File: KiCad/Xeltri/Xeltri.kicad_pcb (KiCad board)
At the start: 6 copper layers, 100 x 100 mm, 188 parts, among them J1 PJ-035DH, J2 877159106, J3 HR911105A_C12074, Q1 AOD407, U1 XC7A35T-CSG325, U10 SY8843QWC, U11 RT9013-18GB, U12 RT9013-12GB, U13 TPS22966DPUR, U14 TPS22966DPUR, U15 TPS22966DPUR, U16 TPS22966DPUR, U17 CH334P, U2 V851S, U3 TPS56637RPAR, U4 TPS56637RPAR, U5 STM32H745XIHx, U6 RTL8201F-VB-CG, U7 SY8843QWC, U8 SY8843QWC, U9 SY8843QWC, Y1 25Mhz

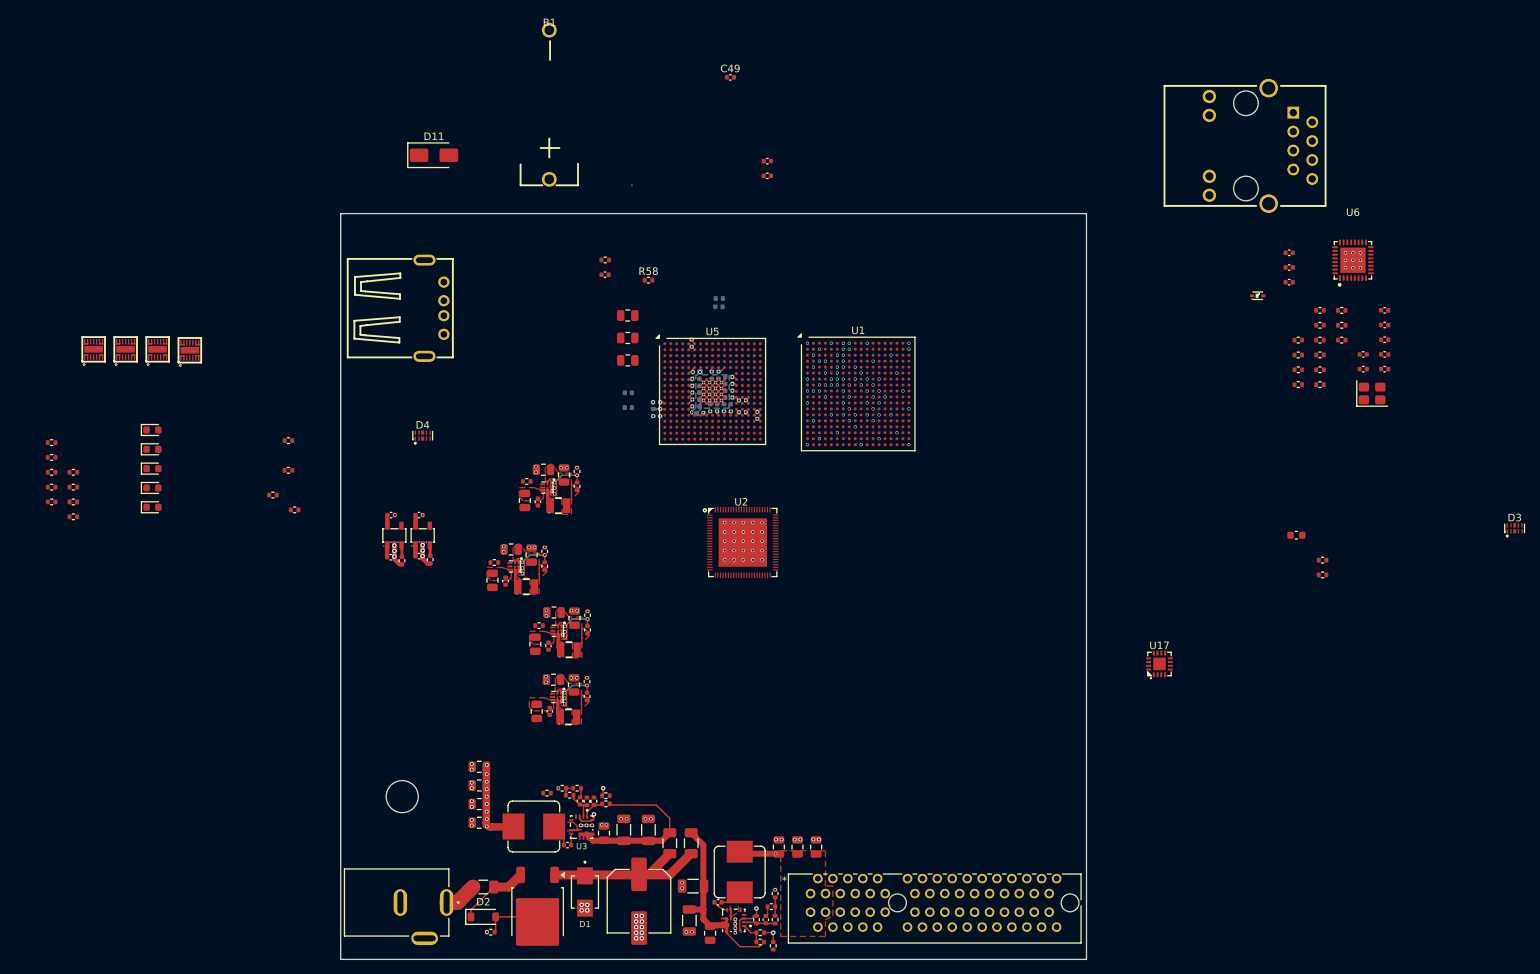
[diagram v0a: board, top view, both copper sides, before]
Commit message: Lay out STM32 power decoupling and add USB FS plus 24 V CIN ceramics.
USB VDD33/VDD50 share local 100 nF + 1 µF on 3.3 V; VBAT keeps a local 100 nF until the cell and diode are placed.

Co-authored-by: Cursor <cursoragent@cursor.com>
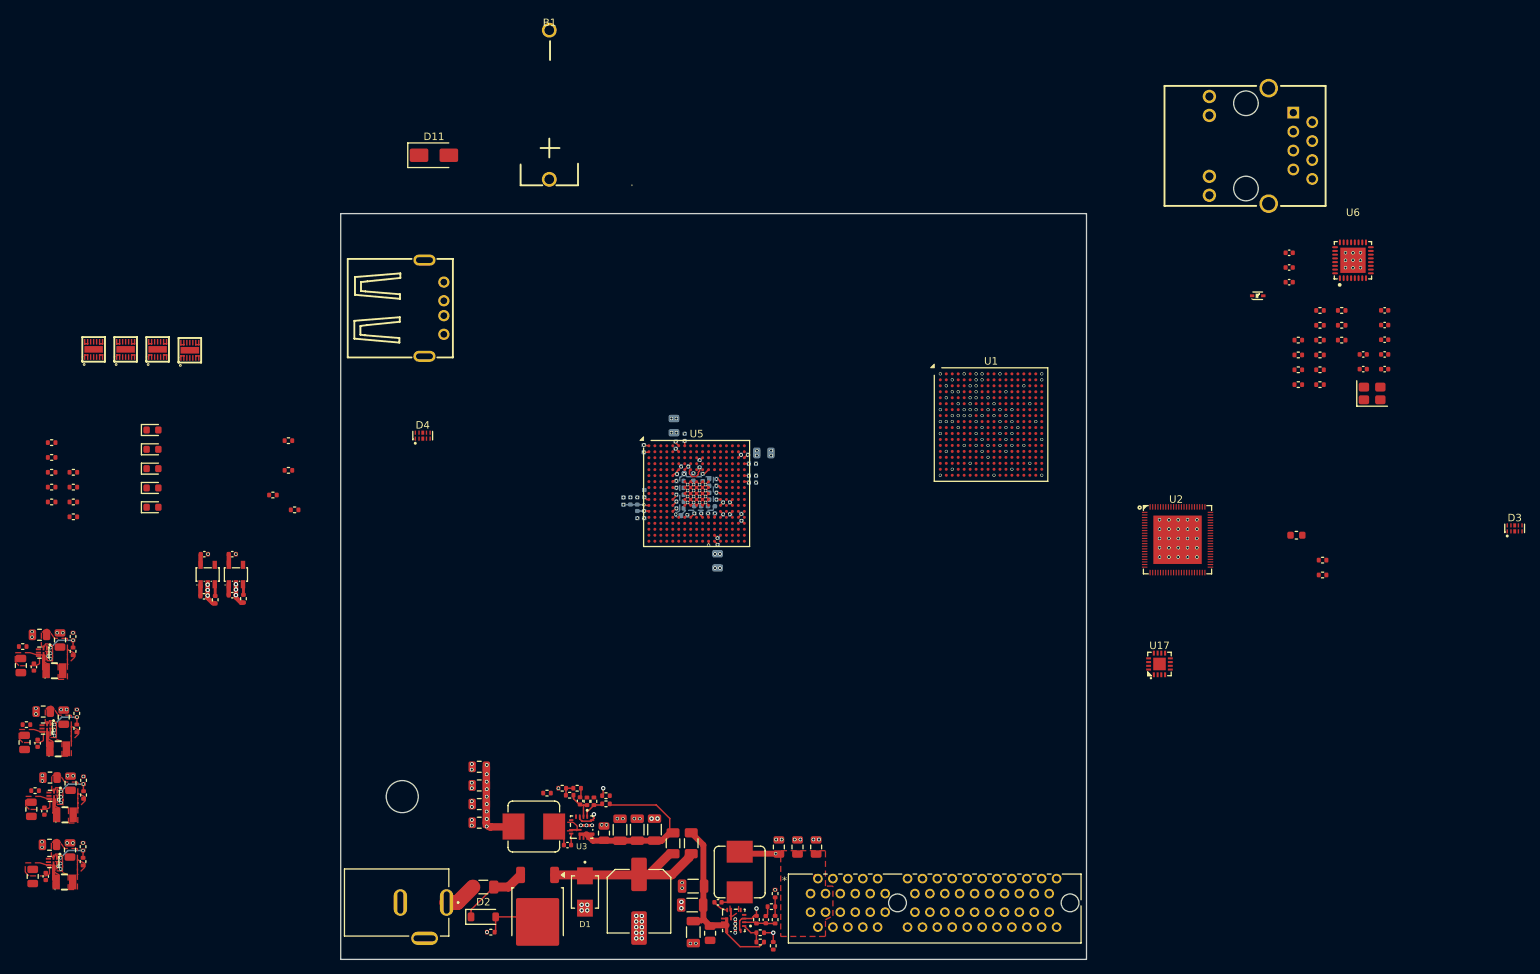
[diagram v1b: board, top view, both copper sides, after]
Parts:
- added C83: 10uF/50V, Capacitor_SMD:C_1206_3216Metric, F.Cu at (140.9, 138.5)
- added C84: 10uF/50V, Capacitor_SMD:C_1206_3216Metric, F.Cu at (135.8, 128.4)
- added C85: 100nF/16V, Capacitor_SMD:C_0402_1005Metric, B.Cu at (149.0, 81.0)
- added C86: 1uF/25V, Capacitor_SMD:C_0402_1005Metric, B.Cu at (149.0, 81.9)
- C49, C53, C54, C76, C77, C78, C82, R58, R61: moved to B.Cu
- moved C32 71.1 mm to (52.3, 125.7)
- moved C33 71.1 mm to (54.0, 125.9)
- moved C34 71.1 mm to (57.5, 122.2)
- moved C46 71.1 mm to (54.8, 121.4)
- moved L4 71.1 mm to (56.8, 126.4)
- moved R34 71.1 mm to (59.3, 121.8)
- moved R53 71.1 mm to (52.8, 123.2)
- moved U8 71.1 mm to (55.3, 123.8)
- moved C29 71.1 mm to (57.5, 131.2)
- moved C30 71.1 mm to (54.2, 134.7)
- moved C31 71.1 mm to (52.5, 134.7)
- moved C38 71.1 mm to (50.9, 106.4)
- moved C39 71.1 mm to (52.6, 106.6)
- moved C40 71.1 mm to (56.1, 103.0)
- moved C45 71.1 mm to (54.7, 130.5)
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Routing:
- net Net-(U5-BOOT0): track 0.00 -> 3.13 mm, vias 0 -> 1
- net VDDA: track 0.68 -> 3.45 mm, vias 1 -> 2
- net +3.3V: track 14.0 -> 16.5 mm, vias 22 -> 33
- net GND: track 45.2 -> 47.5 mm, vias 219 -> 239
- net Net-(C50-Pad2): track 0.00 -> 1.79 mm, vias 0 -> 3
- net Net-(U5-NRST): track 0.00 -> 0.72 mm, vias 0 -> 1
- net Net-(D11-K): track 0.00 -> 0.71 mm, vias 0 -> 1
- net Net-(U5-PDR_ON): track 0.00 -> 0.64 mm, vias 0 -> 1
- added copper zone on In3.Cu, net +3.3V
- added copper zone on In3.Cu, net Net-(C50-Pad2)

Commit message: Match the six-layer stackup to JLC06161H-3313 and update FPGA power wiring.
Co-authored-by: Cursor <cursoragent@cursor.com>
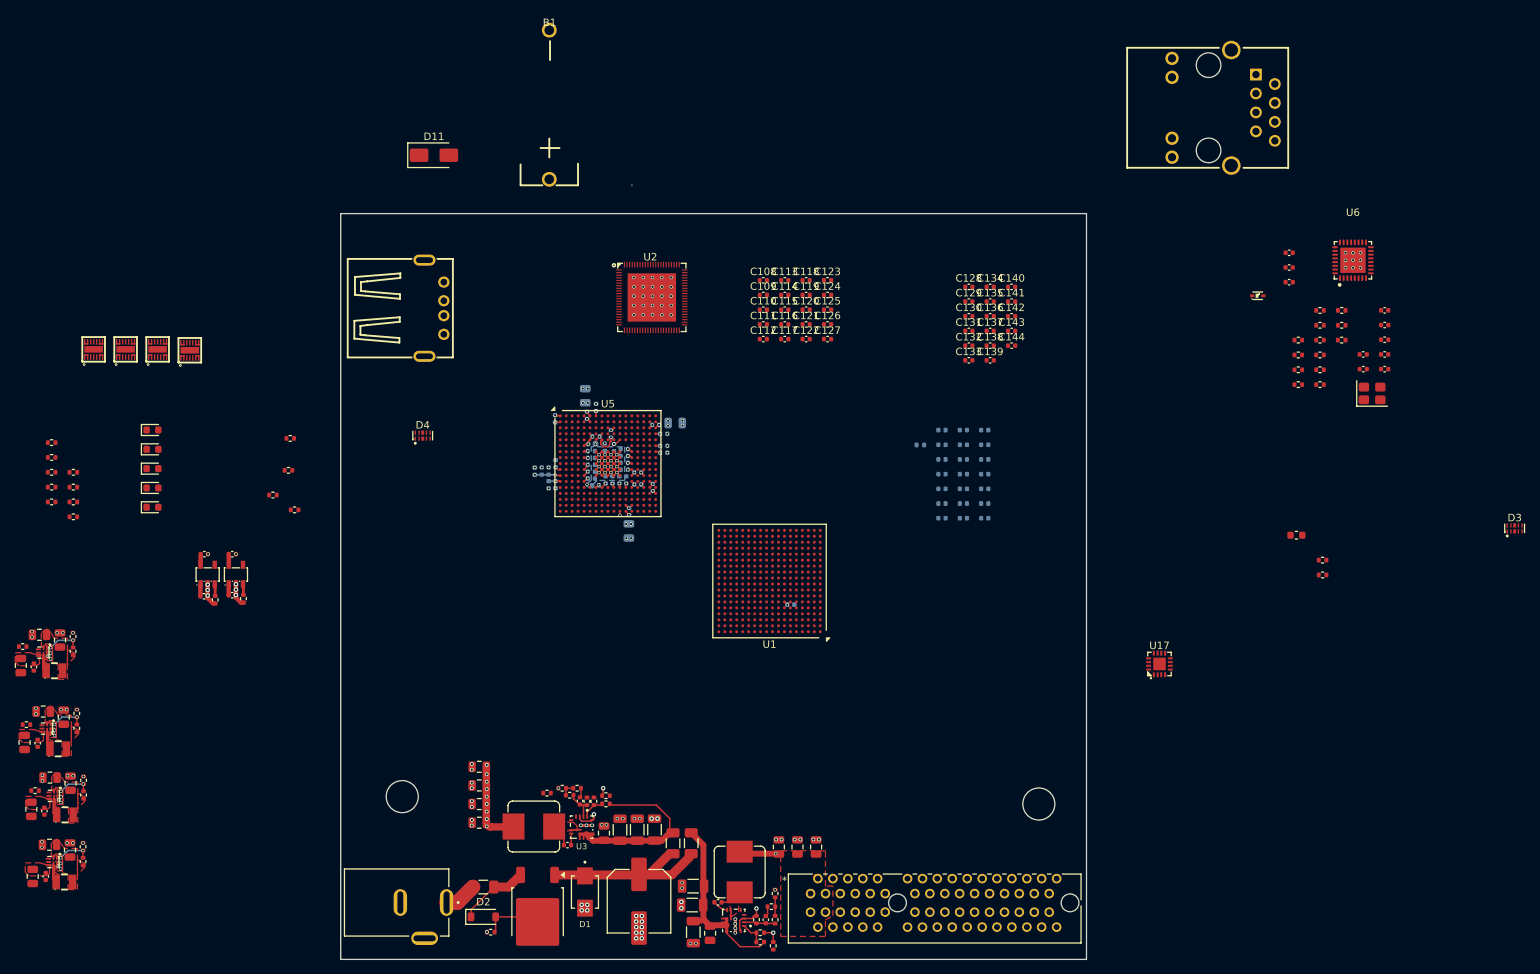
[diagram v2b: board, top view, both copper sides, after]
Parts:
- added C100: 470nF, Capacitor_SMD:C_0402_1005Metric, B.Cu at (177.2, 86.7)
- added C101: 470nF, Capacitor_SMD:C_0402_1005Metric, B.Cu at (174.4, 74.8)
- added C102: 470nF, Capacitor_SMD:C_0402_1005Metric, B.Cu at (174.4, 76.8)
- added C103: 470nF, Capacitor_SMD:C_0402_1005Metric, B.Cu at (174.4, 78.8)
- added C104: 470nF, Capacitor_SMD:C_0402_1005Metric, B.Cu at (174.4, 80.8)
- added C105: 470nF, Capacitor_SMD:C_0402_1005Metric, B.Cu at (174.4, 82.7)
- added C106: 470nF, Capacitor_SMD:C_0402_1005Metric, B.Cu at (174.4, 84.7)
- added C107: 470nF, Capacitor_SMD:C_0402_1005Metric, B.Cu at (174.4, 86.7)
- added C108: 470nF, Capacitor_SMD:C_0402_1005Metric, F.Cu at (150.4, 54.8)
- added C109: 470nF, Capacitor_SMD:C_0402_1005Metric, F.Cu at (150.4, 56.7)
- added C110: 470nF, Capacitor_SMD:C_0402_1005Metric, F.Cu at (150.4, 58.7)
- added C111: 470nF, Capacitor_SMD:C_0402_1005Metric, F.Cu at (150.4, 60.7)
- added C112: 470nF, Capacitor_SMD:C_0402_1005Metric, F.Cu at (150.4, 62.6)
- added C113: 470nF, Capacitor_SMD:C_0402_1005Metric, F.Cu at (153.3, 54.8)
- added C114: 470nF, Capacitor_SMD:C_0402_1005Metric, F.Cu at (153.3, 56.7)
- added C115: 470nF, Capacitor_SMD:C_0402_1005Metric, F.Cu at (153.3, 58.7)
- added C116: 470nF, Capacitor_SMD:C_0402_1005Metric, F.Cu at (153.3, 60.7)
- added C117: 470nF, Capacitor_SMD:C_0402_1005Metric, F.Cu at (153.3, 62.6)
- added C118: 470nF, Capacitor_SMD:C_0402_1005Metric, F.Cu at (156.2, 54.8)
- added C119: 470nF, Capacitor_SMD:C_0402_1005Metric, F.Cu at (156.2, 56.7)
- added C120: 470nF, Capacitor_SMD:C_0402_1005Metric, F.Cu at (156.2, 58.7)
- added C121: 470nF, Capacitor_SMD:C_0402_1005Metric, F.Cu at (156.2, 60.7)
- added C122: 470nF, Capacitor_SMD:C_0402_1005Metric, F.Cu at (156.2, 62.6)
- added C123: 470nF, Capacitor_SMD:C_0402_1005Metric, F.Cu at (159.0, 54.8)
- added C124: 470nF, Capacitor_SMD:C_0402_1005Metric, F.Cu at (159.0, 56.7)
- added C125: 470nF, Capacitor_SMD:C_0402_1005Metric, F.Cu at (159.0, 58.7)
- added C126: 470nF, Capacitor_SMD:C_0402_1005Metric, F.Cu at (159.0, 60.7)
- added C127: 470nF, Capacitor_SMD:C_0402_1005Metric, F.Cu at (159.0, 62.6)
- added C128: 470nF, Capacitor_SMD:C_0402_1005Metric, F.Cu at (178.0, 55.6)
- added C129: 470nF, Capacitor_SMD:C_0402_1005Metric, F.Cu at (178.0, 57.6)
- added C130: 470nF, Capacitor_SMD:C_0402_1005Metric, F.Cu at (178.0, 59.6)
- added C131: 470nF, Capacitor_SMD:C_0402_1005Metric, F.Cu at (178.0, 61.6)
- added C132: 470nF, Capacitor_SMD:C_0402_1005Metric, F.Cu at (178.0, 63.5)
- added C133: 470nF, Capacitor_SMD:C_0402_1005Metric, F.Cu at (178.0, 65.5)
- added C134: 470nF, Capacitor_SMD:C_0402_1005Metric, F.Cu at (180.8, 55.6)
- added C135: 470nF, Capacitor_SMD:C_0402_1005Metric, F.Cu at (180.8, 57.6)
- added C136: 470nF, Capacitor_SMD:C_0402_1005Metric, F.Cu at (180.8, 59.6)
- added C137: 470nF, Capacitor_SMD:C_0402_1005Metric, F.Cu at (180.8, 61.6)
- added C138: 470nF, Capacitor_SMD:C_0402_1005Metric, F.Cu at (180.8, 63.5)
- added C139: 470nF, Capacitor_SMD:C_0402_1005Metric, F.Cu at (180.8, 65.5)
- added C140: 470nF, Capacitor_SMD:C_0402_1005Metric, F.Cu at (183.7, 55.6)
- added C141: 470nF, Capacitor_SMD:C_0402_1005Metric, F.Cu at (183.7, 57.6)
- added C142: 470nF, Capacitor_SMD:C_0402_1005Metric, F.Cu at (183.7, 59.6)
- added C143: 470nF, Capacitor_SMD:C_0402_1005Metric, F.Cu at (183.7, 61.6)
- added C144: 470nF, Capacitor_SMD:C_0402_1005Metric, F.Cu at (183.7, 63.5)
- added C87: 470nF, Capacitor_SMD:C_0402_1005Metric, B.Cu at (180.1, 74.8)
- added C88: 470nF, Capacitor_SMD:C_0402_1005Metric, B.Cu at (180.1, 76.8)
- added C89: 470nF, Capacitor_SMD:C_0402_1005Metric, B.Cu at (180.1, 78.8)
- added C90: 470nF, Capacitor_SMD:C_0402_1005Metric, B.Cu at (180.1, 80.8)
- added C91: 470nF, Capacitor_SMD:C_0402_1005Metric, B.Cu at (180.1, 82.7)
- added C92: 470nF, Capacitor_SMD:C_0402_1005Metric, B.Cu at (180.1, 84.7)
- added C93: 470nF, Capacitor_SMD:C_0402_1005Metric, B.Cu at (180.1, 86.7)
- added C94: 470nF, Capacitor_SMD:C_0402_1005Metric, B.Cu at (177.2, 74.8)
- added C95: 470nF, Capacitor_SMD:C_0402_1005Metric, B.Cu at (177.2, 76.8)
- added C96: 470nF, Capacitor_SMD:C_0402_1005Metric, B.Cu at (177.2, 78.8)
- added C97: 470nF, Capacitor_SMD:C_0402_1005Metric, B.Cu at (177.2, 80.8)
- added C98: 470nF, Capacitor_SMD:C_0402_1005Metric, B.Cu at (177.2, 82.7)
- added C99: 470nF, Capacitor_SMD:C_0402_1005Metric, B.Cu at (177.2, 84.7)
- added FB3: 600R@100M, Inductor_SMD:L_0402_1005Metric, B.Cu at (154.1, 98.3)
- added R59: 100R, Resistor_SMD:R_0402_1005Metric, B.Cu at (171.5, 76.8)
- added REF**: MountingHole_4.3mm_M4, MountingHole:MountingHole_4.3mm_M4, F.Cu at (187.4, 125.0)
- moved U2 77.6 mm to (135.3, 57.1)
- moved U1 36.4 mm to (151.2, 95.1), turned to 180 degrees
- moved C50 12.5 mm to (128.0, 71.8)
- moved C54 12.5 mm to (120.7, 80.3)
- moved C56 12.5 mm to (130.4, 77.2)
- moved C57 12.5 mm to (131.8, 77.4)
- moved C64 12.5 mm to (131.1, 81.5)
- moved C66 12.5 mm to (129.3, 81.5)
- moved C67 12.5 mm to (127.9, 82.3)
- moved C78 12.5 mm to (132.4, 88.4)
- moved C81 12.5 mm to (136.0, 74.2)
- moved U5 12.5 mm to (129.6, 79.3)
- moved C58 12.5 mm to (131.8, 78.3)
- moved C59 12.5 mm to (131.8, 79.2)
- moved C60 12.5 mm to (131.8, 80.2)
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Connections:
- U1 pad A16: unconnected-(U1A-VCCO_15-PadA16) -> FPGA_3.3V
- U1 pad A2: unconnected-(U1D-MGTAVTT-PadA2) -> FPGA_1V2
- U1 pad A6: unconnected-(U1D-MGTRREF_216-PadA6) -> Net-(U1D-MGTRREF_216)
- U1 pad B13: unconnected-(U1A-VCCO_15-PadB13) -> FPGA_3.3V
- U1 pad B4: unconnected-(U1D-MGTAVCC-PadB4) -> FPGA_MGTAVCC
- U1 pad C1: unconnected-(U1D-MGTAVTT-PadC1) -> FPGA_1V2
- U1 pad C10: unconnected-(U1A-VCCO_15-PadC10) -> FPGA_3.3V
- U1 pad C5: unconnected-(U1D-MGTAVCC-PadC5) -> FPGA_MGTAVCC
- U1 pad D17: unconnected-(U1A-VCCO_15-PadD17) -> FPGA_3.3V
- U1 pad E1: unconnected-(U1D-MGTAVTT-PadE1) -> FPGA_1V2
- U1 pad E10: unconnected-(U1E-VCCO_0-PadE10) -> FPGA_3.3V
- U1 pad E11: unconnected-(U1F-VCCBATT_0-PadE11) -> FPGA_1V8
- U1 pad E14: unconnected-(U1A-VCCO_15-PadE14) -> FPGA_3.3V
- U1 pad E5: unconnected-(U1D-MGTAVCC-PadE5) -> FPGA_MGTAVCC
- U1 pad F11: unconnected-(U1F-VCCBRAM-PadF11) -> FPGA_1V0
- U1 pad F3: unconnected-(U1D-MGTAVTT-PadF3) -> FPGA_1V2
- U1 pad F5: unconnected-(U1D-MGTAVCC-PadF5) -> FPGA_MGTAVCC
- U1 pad F7: unconnected-(U1F-VCCINT-PadF7) -> FPGA_1V0
- U1 pad F9: unconnected-(U1F-VCCINT-PadF9) -> FPGA_1V0
- U1 pad G10: unconnected-(U1F-VCCBRAM-PadG10) -> FPGA_1V0
- U1 pad G12: unconnected-(U1F-VCCAUX-PadG12) -> FPGA_1V8
- U1 pad G18: unconnected-(U1A-VCCO_15-PadG18) -> FPGA_3.3V
- U1 pad G2: unconnected-(U1D-MGTAVTT-PadG2) -> FPGA_1V2
- U1 pad G8: unconnected-(U1F-VCCINT-PadG8) -> FPGA_1V0
- U1 pad H11: unconnected-(U1F-VCCBRAM-PadH11) -> FPGA_1V0
- U1 pad H13: unconnected-(U1F-VCCAUX-PadH13) -> FPGA_1V8
- U1 pad H15: unconnected-(U1A-VCCO_15-PadH15) -> FPGA_3.3V
- U1 pad H7: unconnected-(U1F-VCCINT-PadH7) -> FPGA_1V0
- U1 pad H9: unconnected-(U1F-VCCINT-PadH9) -> FPGA_1V0
- U1 pad J10: unconnected-(U1F-VCCADC_0-PadJ10) -> FPGA_1V8
- U1 pad J12: unconnected-(U1F-VCCINT-PadJ12) -> FPGA_1V0
- U1 pad J8: unconnected-(U1F-VCCINT-PadJ8) -> FPGA_1V0
- U1 pad J9: unconnected-(U1F-GNDADC_0-PadJ9) -> GND
- U1 pad K11: unconnected-(U1F-VCCINT-PadK11) -> FPGA_1V0
- U1 pad K13: unconnected-(U1F-VCCAUX-PadK13) -> FPGA_1V8
- U1 pad K7: unconnected-(U1F-VCCINT-PadK7) -> FPGA_1V0
- U1 pad L12: unconnected-(U1F-VCCINT-PadL12) -> FPGA_1V0
- U1 pad L16: unconnected-(U1A-VCCO_14-PadL16) -> FPGA_3.3V
- U1 pad L6: unconnected-(U1B-VCCO_34-PadL6) -> FPGA_3.3V
- U1 pad L8: unconnected-(U1F-VCCINT-PadL8) -> FPGA_1V0
- U1 pad M11: unconnected-(U1F-VCCINT-PadM11) -> FPGA_1V0
- U1 pad M13: unconnected-(U1F-VCCAUX-PadM13) -> FPGA_1V8
- U1 pad M3: unconnected-(U1B-VCCO_34-PadM3) -> FPGA_3.3V
- U1 pad M7: unconnected-(U1F-VCCINT-PadM7) -> FPGA_1V0
- U1 pad N10: unconnected-(U1F-VCCINT-PadN10) -> FPGA_1V0
- U1 pad N12: unconnected-(U1F-VCCINT-PadN12) -> FPGA_1V0
- U1 pad N8: unconnected-(U1F-VCCINT-PadN8) -> FPGA_1V0
- U1 pad P11: unconnected-(U1F-VCCINT-PadP11) -> FPGA_1V0
- U1 pad P13: unconnected-(U1F-VCCAUX-PadP13) -> FPGA_1V8
- U1 pad P17: unconnected-(U1A-VCCO_14-PadP17) -> FPGA_3.3V
- U1 pad P7: unconnected-(U1B-VCCO_34-PadP7) -> FPGA_3.3V
- U1 pad P9: unconnected-(U1F-VCCINT-PadP9) -> FPGA_1V0
- U1 pad R10: unconnected-(U1E-VCCO_0-PadR10) -> FPGA_3.3V
- U1 pad R14: unconnected-(U1A-VCCO_14-PadR14) -> FPGA_3.3V
- U1 pad R4: unconnected-(U1B-VCCO_34-PadR4) -> FPGA_3.3V
- U1 pad T1: unconnected-(U1B-VCCO_34-PadT1) -> FPGA_3.3V
- U1 pad T11: unconnected-(U1A-VCCO_14-PadT11) -> FPGA_3.3V
- U1 pad U18: unconnected-(U1A-VCCO_14-PadU18) -> FPGA_3.3V
- U1 pad U8: unconnected-(U1A-VCCO_14-PadU8) -> FPGA_3.3V
- U1 pad V15: unconnected-(U1A-VCCO_14-PadV15) -> FPGA_3.3V
- U1 pad V5: unconnected-(U1B-VCCO_34-PadV5) -> FPGA_3.3V
- U13 pad 11: unconnected-(U13-GND-Pad11) -> GND
- U13 pad 15: unconnected-(U13-EP-Pad15) -> GND
- U13 pad 4: +3.3V -> +5V
- U14 pad 11: unconnected-(U14-GND-Pad11) -> GND
- U14 pad 15: unconnected-(U14-EP-Pad15) -> GND
- U14 pad 4: +3.3V -> +5V
- U15 pad 11: unconnected-(U15-GND-Pad11) -> GND
- U15 pad 15: unconnected-(U15-EP-Pad15) -> GND
- U15 pad 4: unconnected-(U15-VBIAS-Pad4) -> +5V
- U16 pad 11: unconnected-(U16-GND-Pad11) -> GND
- U16 pad 15: unconnected-(U16-EP-Pad15) -> GND
- U16 pad 4: unconnected-(U16-VBIAS-Pad4) -> +5V
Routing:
- net FPGA_1V0: track 0.00 -> 0.55 mm, vias 0 -> 1
- net GND: vias 239 -> 164
- added copper zone on In4.Cu, net +3.3V
- added copper zone on In3.Cu, net GND
- added copper zone on In4.Cu, net Net-(C50-Pad2)
- removed copper zone on In3.Cu, net +3.3V
- removed copper zone on In4.Cu, net GND
- removed copper zone on In3.Cu, net Net-(C50-Pad2)
